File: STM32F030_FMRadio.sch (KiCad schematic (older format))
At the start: 17 parts, among them J1 Conn_01x04_Female, J2 Screw_Terminal_01x02, J3 AudioJack3_Ground, SW1 Rotary_Encoder_Switch, U1 LP5907MFX-3.3, U2 STM32F030F4Px, U3 TEA5767

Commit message: + pull_Up encoder, разведена ПП
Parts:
- removed J3: AudioJack3_Ground, Connector_Audio:Jack_3.5mm_CUI_SJ-3524-SMT_Horizontal, symbol Connector:AudioJack3_Ground
- added J3: Conn_01x04, Connector_PinHeader_2.54mm:PinHeader_1x04_P2.54mm_Vertical, symbol Connector_Generic:Conn_01x04
- added J4: Conn_01x05, Connector_PinHeader_2.54mm:PinHeader_1x05_P2.54mm_Vertical, symbol Connector_Generic:Conn_01x05
- added R3, R4: R, Resistor_SMD:R_0805_2012Metric, symbol Device:R
- U3: symbol tea5767:TEA5767 -> STM32F030_FMRadio-rescue:TEA5767-tea5767
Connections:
- net labels added: NRST, SWCLK, SWDIO, VCC
- wire segments 80 -> 94
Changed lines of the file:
@@
 EESchema Schematic File Version 4
-EELAYER 30 0
+LIBS:STM32F030_FMRadio-cache
+EELAYER 29 0
 EELAYER END
 $Descr A4 11693 8268
@@
 $EndComp
 $Comp
-L tea5767:TEA5767 U3
+L STM32F030_FMRadio-rescue:TEA5767-tea5767 U3
 U 1 1 5E2C6CF2
 P 7800 3650
@@
 	3250 1950 3600 1950
 Wire Wire Line
-	5000 1950 5000 2450
+	5000 1950 5000 2200
 Wire Wire Line
 	4900 2450 4900 1950
 Connection ~ 4900 1950
-Wire Wire Line
-	4900 1950 5000 1950
 Wire Wire Line
 	3950 2150 3950 1950
@@
 Wire Wire Line
 	2100 1950 1950 1950
-$Comp
-L Connector:AudioJack3_Ground J3
-U 1 1 5E35D311
-P 9350 3700
-F 0 "J3" H 9070 3576 50  0000 R CNN
-F 1 "AudioJack3_Ground" H 9070 3667 50  0000 R CNN
-F 2 "Connector_Audio:Jack_3.5mm_CUI_SJ-3524-SMT_Horizontal" H 9350 3700 50  0001 C CNN
-F 3 "~" H 9350 3700 50  0001 C CNN
-	1    9350 3700
-	-1   0    0    1
-$EndComp
-Wire Wire Line
-	9350 3400 9700 3400
-Wire Wire Line
-	9700 3400 9700 4250
-Wire Wire Line
-	9700 4250 9150 4250
 Wire Wire Line
 	9150 3800 9150 4250
@@
 Wire Wire Line
 	8300 4250 9150 4250
-Connection ~ 9150 4250
 $Comp
 L Device:C C6
@@
 	1600 2550 1950 2550
 Connection ~ 1950 2550
+Wire Wire Line
+	5400 3650 5800 3650
+Wire Wire Line
+	5400 3750 5800 3750
+$Comp
+L Connector_Generic:Conn_01x05 J4
+U 1 1 5E330109
+P 2800 3650
+F 0 "J4" H 2950 3600 50  0000 L CNN
+F 1 "Conn_01x05" H 2950 3500 50  0000 L CNN
+F 2 "Connector_PinHeader_2.54mm:PinHeader_1x05_P2.54mm_Vertical" H 2800 3650 50  0001 C CNN
+F 3 "~" H 2800 3650 50  0001 C CNN
+	1    2800 3650
+	1    0    0    -1
+$EndComp
+$Comp
+L power:GND #PWR07
+U 1 1 5E3326C0
+P 2550 3950
+F 0 "#PWR07" H 2550 3700 50  0001 C CNN
+F 1 "GND" H 2555 3777 50  0000 C CNN
+F 2 "" H 2550 3950 50  0001 C CNN
+F 3 "" H 2550 3950 50  0001 C CNN
+	1    2550 3950
+	1    0    0    -1
+$EndComp
+Wire Wire Line
+	2600 3850 2550 3850
+Wire Wire Line
+	2550 3850 2550 3950
+Wire Wire Line
+	2600 3450 2550 3450
+Wire Wire Line
+	2550 3450 2550 3250
+Text Label 2550 3350 0    50   ~ 0
++3V3
+Text Label 4150 2650 0    50   ~ 0
+NRST
+Wire Wire Line
+	2600 3550 2400 3550
+Wire Wire Line
+	2600 3650 2400 3650
+Wire Wire Line
+	2600 3750 2400 3750
+Text Label 5650 3650 0    50   ~ 0
+SWDIO
+Text Label 2400 3650 0    50   ~ 0
+SWDIO
+Text Label 2400 3550 0    50   ~ 0
+NRST
+Text Label 2400 3750 0    50   ~ 0
+SWCLK
+Text Label 5650 3750 0    50   ~ 0
+SWCLK
+$Comp
+L Connector_Generic:Conn_01x04 J3
+U 1 1 5E345962
+P 9350 3600
+F 0 "J3" H 9430 3592 50  0000 L CNN
+F 1 "Conn_01x04" H 9430 3501 50  0000 L CNN
+F 2 "Connector_PinHeader_2.54mm:PinHeader_1x04_P2.54mm_Vertical" H 9350 3600 50  0001 C CNN
+F 3 "~" H 9350 3600 50  0001 C CNN
+	1    9350 3600
+	1    0    0    -1
+$EndComp
+Wire Wire Line
+	9050 3050 9050 3500
+Wire Wire Line
+	9050 3500 9150 3500
+Text Label 1800 1950 0    50   ~ 0
+VCC
+$Comp
+L Device:R R3
+U 1 1 5E395E25
+P 5250 1950
+F 0 "R3" V 5043 1950 50  0000 C CNN
+F 1 "R" V 5134 1950 50  0000 C CNN
+F 2 "Resistor_SMD:R_0805_2012Metric" V 5180 1950 50  0001 C CNN
+F 3 "~" H 5250 1950 50  0001 C CNN
+	1    5250 1950
+	0    1    1    0
+$EndComp
+$Comp
+L Device:R R4
+U 1 1 5E396085
+P 5250 2200
+F 0 "R4" V 5043 2200 50  0000 C CNN
+F 1 "R" V 5134 2200 50  0000 C CNN
+F 2 "Resistor_SMD:R_0805_2012Metric" V 5180 2200 50  0001 C CNN
+F 3 "~" H 5250 2200 50  0001 C CNN
+	1    5250 2200
+	0    1    1    0
+$EndComp
+Wire Wire Line
+	5400 1950 5550 1950
+Wire Wire Line
+	5550 1950 5550 2000
+Connection ~ 5550 2000
+Wire Wire Line
+	4900 1950 5000 1950
+Wire Wire Line
+	5100 1950 5000 1950
+Wire Wire Line
+	5100 2200 5000 2200
+Connection ~ 5000 2200
+Wire Wire Line
+	5000 2200 5000 2450
+Wire Wire Line
+	5400 2200 5600 2200
+Connection ~ 5600 2200
 $EndSCHEMATC

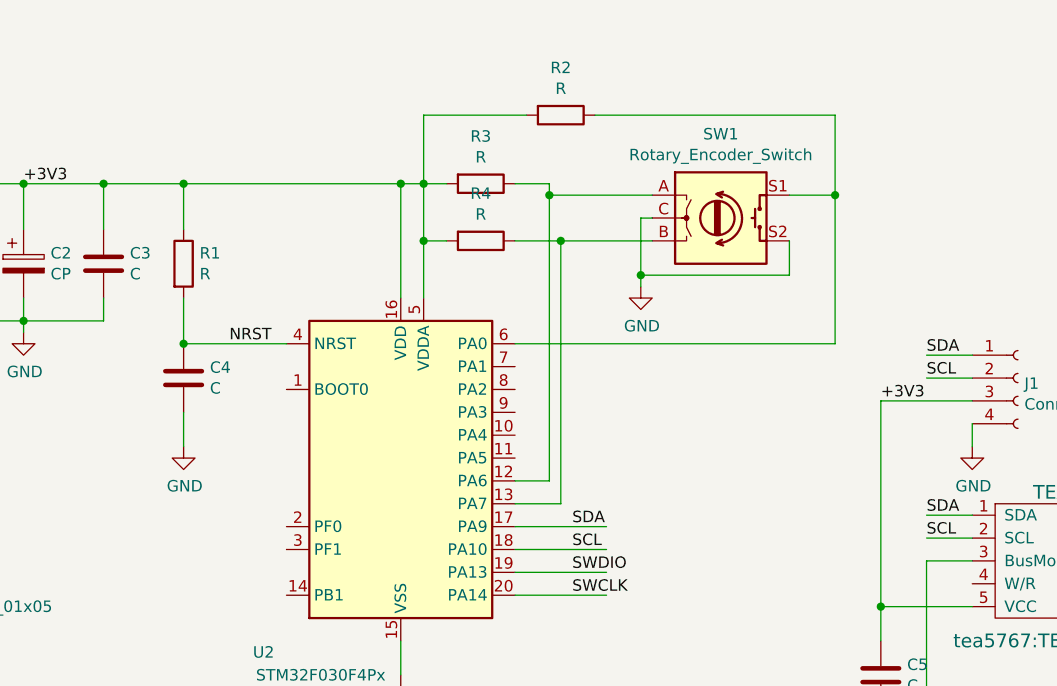
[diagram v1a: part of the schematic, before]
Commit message: добавлена подтяжка на I2C, перетрассировка
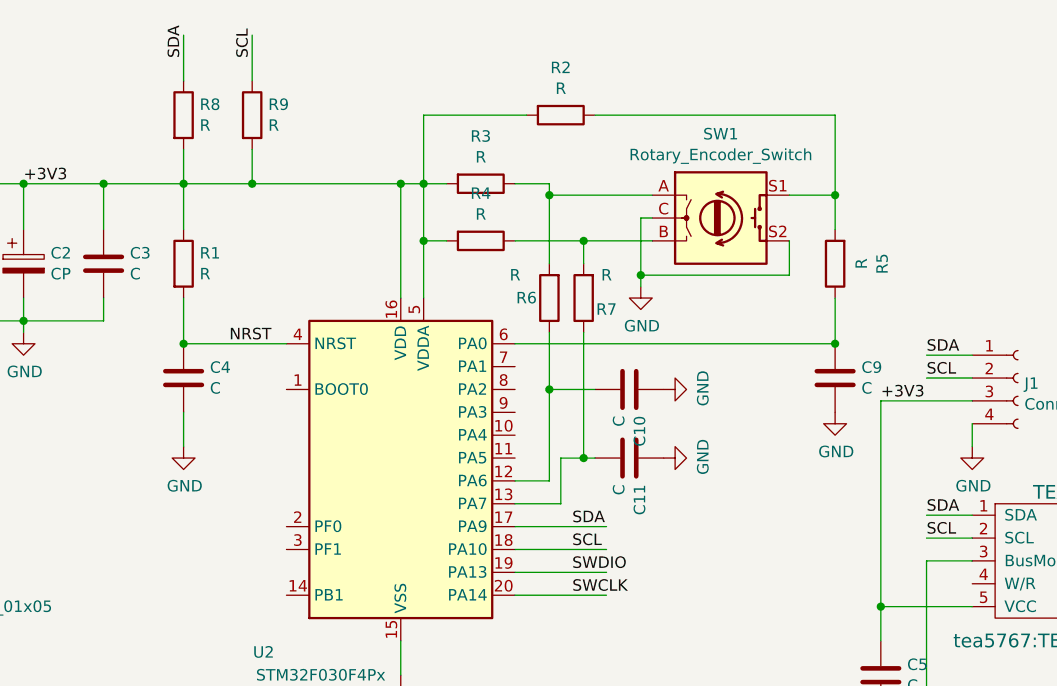
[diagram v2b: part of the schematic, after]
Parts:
- added C10, C11, C9: C, Capacitor_SMD:C_0805_2012Metric, symbol Device:C
- added R5, R6, R7, R8, R9: R, Resistor_SMD:R_0805_2012Metric, symbol Device:R
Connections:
- wire segments 94 -> 107
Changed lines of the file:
@@
 	6000 2000 5550 2000
 Wire Wire Line
-	5550 2000 5550 3250
-Wire Wire Line
 	5550 3250 5400 3250
-Wire Wire Line
-	6000 2200 5600 2200
-Wire Wire Line
-	5600 2200 5600 3350
 Wire Wire Line
 	5600 3350 5400 3350
@@
 Connection ~ 3950 1950
 Wire Wire Line
-	3950 1950 4900 1950
+	3950 1950 4250 1950
 Wire Wire Line
 	3600 2150 3600 1950
@@
 	5950 2100 6000 2100
 Wire Wire Line
-	6800 2000 6800 2650
-Wire Wire Line
 	6800 2650 5400 2650
-Connection ~ 6800 2000
 Text Label 7200 2700 0    50   ~ 0
 SDA
@@
 Wire Wire Line
 	5550 1950 5550 2000
-Connection ~ 5550 2000
 Wire Wire Line
 	4900 1950 5000 1950
@@
 Wire Wire Line
 	5000 2200 5000 2450
-Wire Wire Line
-	5400 2200 5600 2200
-Connection ~ 5600 2200
+$Comp
+L Device:R R5
+U 1 1 5E33ECF4
+P 6800 2300
+F 0 "R5" V 6593 2300 50  0000 C CNN
+F 1 "R" V 6684 2300 50  0000 C CNN
+F 2 "Resistor_SMD:R_0805_2012Metric" V 6730 2300 50  0001 C CNN
+F 3 "~" H 6800 2300 50  0001 C CNN
+	1    6800 2300
+	-1   0    0    1
+$EndComp
+Wire Wire Line
+	6800 2000 6800 2150
+Connection ~ 6800 2000
+Wire Wire Line
+	6800 2450 6800 2650
+$Comp
+L Device:C C9
+U 1 1 5E3446F3
+P 6800 2800
+F 0 "C9" H 6915 2846 50  0000 L CNN
+F 1 "C" H 6915 2755 50  0000 L CNN
+F 2 "Capacitor_SMD:C_0805_2012Metric" H 6838 2650 50  0001 C CNN
+F 3 "~" H 6800 2800 50  0001 C CNN
+	1    6800 2800
+	1    0    0    -1
+$EndComp
+Connection ~ 6800 2650
+$Comp
+L power:GND #PWR08
+U 1 1 5E345466
+P 6800 2950
+F 0 "#PWR08" H 6800 2700 50  0001 C CNN
+F 1 "GND" H 6805 2777 50  0000 C CNN
+F 2 "" H 6800 2950 50  0001 C CNN
+F 3 "" H 6800 2950 50  0001 C CNN
+	1    6800 2950
+	1    0    0    -1
+$EndComp
+$Comp
+L Device:C C11
+U 1 1 5E349F1A
+P 5900 3150
+F 0 "C11" H 6015 3196 50  0000 L CNN
+F 1 "C" H 6015 3105 50  0000 L CNN
+F 2 "Capacitor_SMD:C_0805_2012Metric" H 5938 3000 50  0001 C CNN
+F 3 "~" H 5900 3150 50  0001 C CNN
+	1    5900 3150
+	0    1    1    0
+$EndComp
+$Comp
+L Device:C C10
+U 1 1 5E34AB08
+P 5900 2850
+F 0 "C10" H 6015 2896 50  0000 L CNN
+F 1 "C" H 6015 2805 50  0000 L CNN
+F 2 "Capacitor_SMD:C_0805_2012Metric" H 5938 2700 50  0001 C CNN
+F 3 "~" H 5900 2850 50  0001 C CNN
+	1    5900 2850
+	0    1    1    0
+$EndComp
+Wire Wire Line
+	5750 2850 5550 2850
+Wire Wire Line
+	5550 2850 5550 3250
+Wire Wire Line
+	5750 3150 5700 3150
+Wire Wire Line
+	5600 3150 5600 3350
+$Comp
+L power:GND #PWR09
+U 1 1 5E350757
+P 6050 2850
+F 0 "#PWR09" H 6050 2600 50  0001 C CNN
+F 1 "GND" H 6055 2677 50  0000 C CNN
+F 2 "" H 6050 2850 50  0001 C CNN
+F 3 "" H 6050 2850 50  0001 C CNN
+	1    6050 2850
+	0    -1   -1   0
+$EndComp
+$Comp
+L power:GND #PWR010
+U 1 1 5E353BB1
+P 6050 3150
+F 0 "#PWR010" H 6050 2900 50  0001 C CNN
+F 1 "GND" H 6055 2977 50  0000 C CNN
+F 2 "" H 6050 3150 50  0001 C CNN
+F 3 "" H 6050 3150 50  0001 C CNN
+	1    6050 3150
+	0    -1   -1   0
+$EndComp
+$Comp
+L Device:R R6
+U 1 1 5E354F2D
+P 5550 2450
+F 0 "R6" H 5650 2450 50  0000 C CNN
+F 1 "R" H 5700 2350 50  0000 C CNN
+F 2 "Resistor_SMD:R_0805_2012Metric" V 5480 2450 50  0001 C CNN
+F 3 "~" H 5550 2450 50  0001 C CNN
+	1    5550 2450
+	-1   0    0    1
+$EndComp
+$Comp
+L Device:R R7
+U 1 1 5E3556B4
+P 5700 2450
+F 0 "R7" H 5600 2500 50  0000 C CNN
+F 1 "R" H 5600 2350 50  0000 C CNN
+F 2 "Resistor_SMD:R_0805_2012Metric" V 5630 2450 50  0001 C CNN
+F 3 "~" H 5700 2450 50  0001 C CNN
+	1    5700 2450
+	-1   0    0    1
+$EndComp
+Wire Wire Line
+	5550 2850 5550 2600
+Connection ~ 5550 2850
+Wire Wire Line
+	5700 2600 5700 3150
+Connection ~ 5700 3150
+Wire Wire Line
+	5700 3150 5600 3150
+Wire Wire Line
+	5700 2300 5700 2200
+Connection ~ 5700 2200
+Wire Wire Line
+	5700 2200 6000 2200
+Wire Wire Line
+	5400 2200 5700 2200
+Wire Wire Line
+	5550 2300 5550 2000
+Connection ~ 5550 2000
+$Comp
+L Device:R R8
+U 1 1 5E38B627
+P 3950 1650
+F 0 "R8" H 4020 1696 50  0000 L CNN
+F 1 "R" H 4020 1605 50  0000 L CNN
+F 2 "Resistor_SMD:R_0805_2012Metric" V 3880 1650 50  0001 C CNN
+F 3 "~" H 3950 1650 50  0001 C CNN
+	1    3950 1650
+	1    0    0    -1
+$EndComp
+$Comp
+L Device:R R9
+U 1 1 5E38BA83
+P 4250 1650
+F 0 "R9" H 4320 1696 50  0000 L CNN
+F 1 "R" H 4320 1605 50  0000 L CNN
+F 2 "Resistor_SMD:R_0805_2012Metric" V 4180 1650 50  0001 C CNN
+F 3 "~" H 4250 1650 50  0001 C CNN
+	1    4250 1650
+	1    0    0    -1
+$EndComp
+Wire Wire Line
+	3950 1800 3950 1950
+Wire Wire Line
+	4250 1800 4250 1950
+Connection ~ 4250 1950
+Wire Wire Line
+	4250 1950 4900 1950
+Wire Wire Line
+	3950 1500 3950 1300
+Wire Wire Line
+	4250 1500 4250 1300
+Text Label 3950 1400 1    50   ~ 0
+SDA
+Text Label 4250 1400 1    50   ~ 0
+SCL
 $EndSCHEMATC
